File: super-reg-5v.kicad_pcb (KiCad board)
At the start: 2 copper layers, 85 x 35 mm, 49 parts, among them J1 SENS_IN, Q1 2SA1015GR, Q2 D44H11, U1 LM317T, U3 AD825, X1 AC_IN, X2 DC_OUT

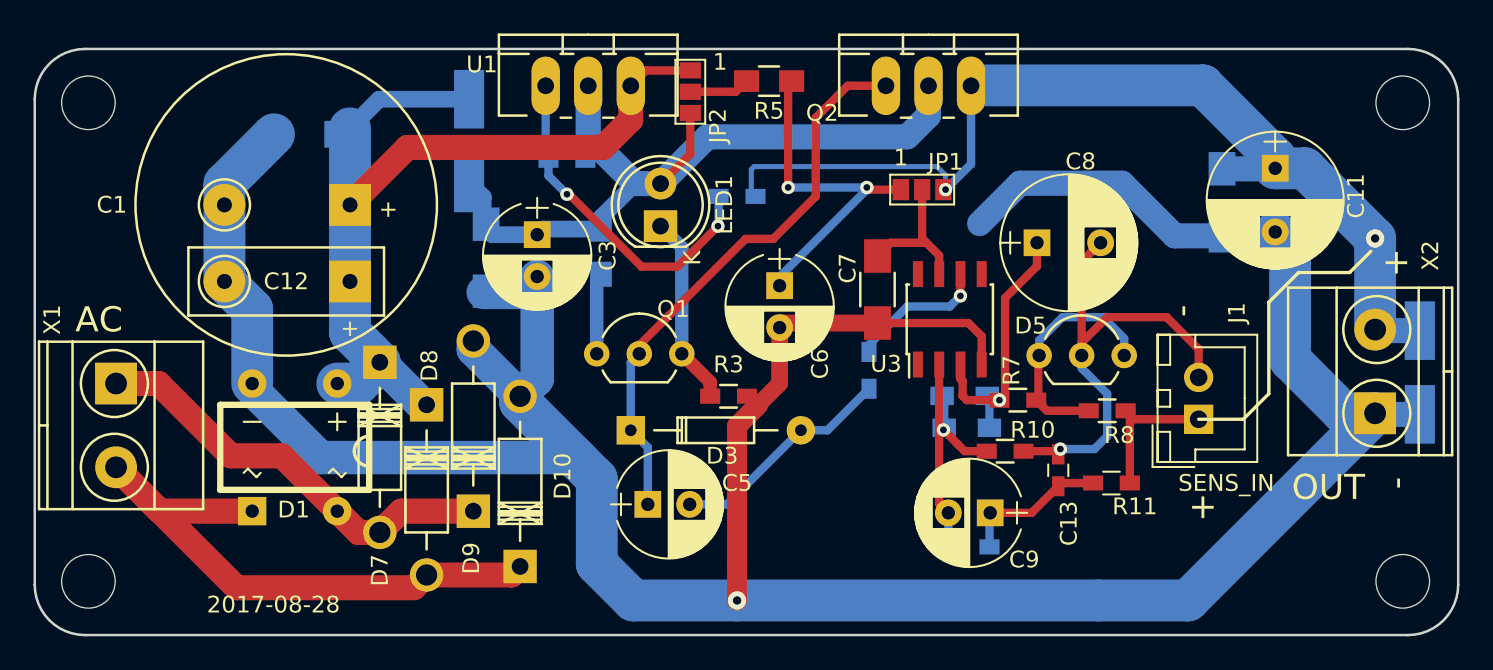
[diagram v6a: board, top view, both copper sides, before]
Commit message: add masks fix silks
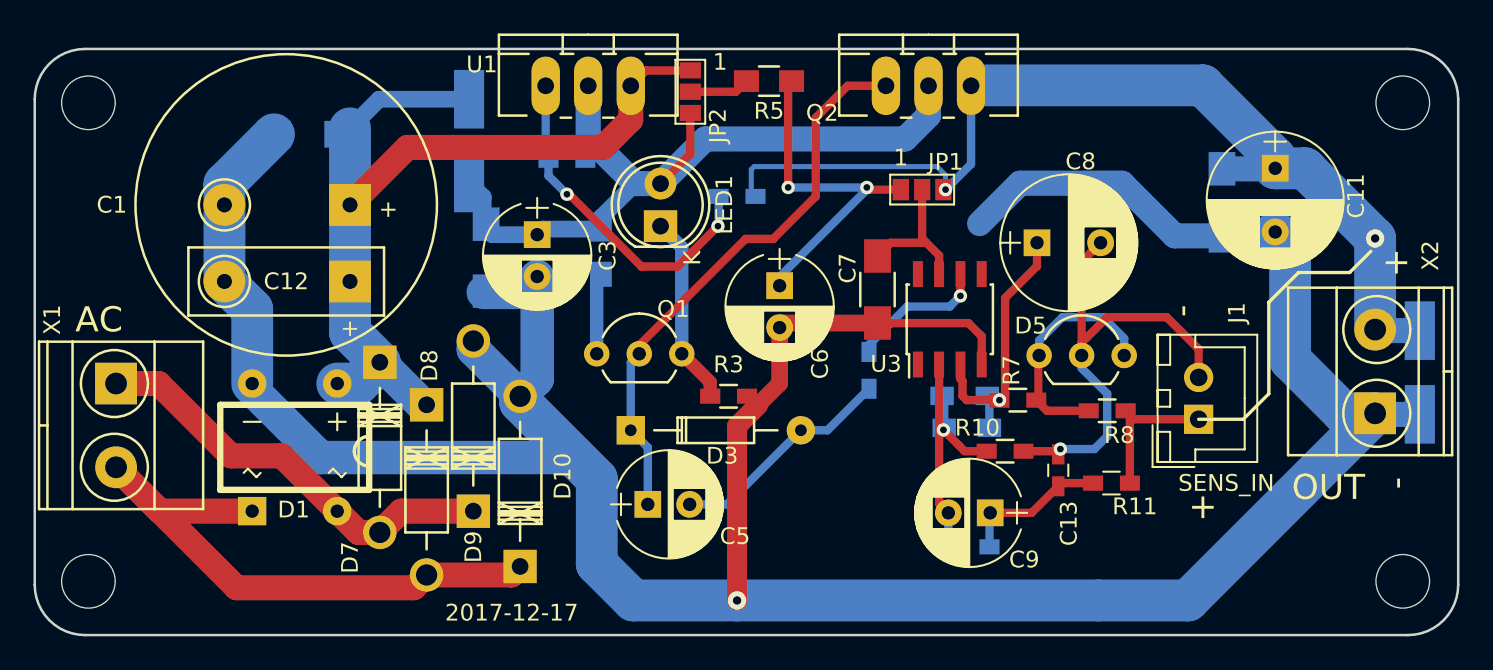
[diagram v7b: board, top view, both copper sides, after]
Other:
- board text added: "2017-12-17"
- board text removed: "2017-08-28"
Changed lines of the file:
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@@
     (area 112.924999 73.924999 198.075001 109.075001)
     (thickness 1.6)
-    (drawings 32)
+    (drawings 80)
     (tracks 247)
     (zones 0)
@@
   )
   (setup
-    (last_trace_width 0.5)
+    (last_trace_width 0.25)
     (user_trace_width 0.3)
     (user_trace_width 0.5)
@@
     (zone_45_only no)
     (trace_min 0.25)
-    (segment_width 1.2)
+    (segment_width 1.5)
     (edge_width 0.15)
     (via_size 0.8)
@@
     (tags "resistor 0603")
     (attr smd)
-    (fp_text reference R1 (at 0.254 1.524 180) (layer B.SilkS)
+    (fp_text reference R1 (at 0.506 1.676 180) (layer B.SilkS)
       (effects (font (size 1 1) (thickness 0.15)) (justify mirror))
     )
@@
     (tags "resistor 0603")
     (attr smd)
-    (fp_text reference R9 (at 0 -1.524 180) (layer B.SilkS)
+    (fp_text reference R9 (at 0 -1.397 180) (layer B.SilkS)
       (effects (font (size 1 1) (thickness 0.15)) (justify mirror))
     )
@@
     (tags "resistor 0603")
     (attr smd)
-    (fp_text reference R10 (at 1.651 -1.27) (layer F.SilkS)
+    (fp_text reference R10 (at -1.651 -1.397) (layer F.SilkS)
       (effects (font (size 1 1) (thickness 0.15)))
     )
@@
     (descr "Diode, DO-41, SOD81, Horizontal, RM 10mm,")
     (tags "Diode, DO-41, SOD81, Horizontal, RM 10mm, 1N4007, SB140,")
-    (fp_text reference D7 (at 12.421 -0.002 270) (layer F.SilkS)
+    (fp_text reference D7 (at 11.659 1.776 270) (layer F.SilkS)
       (effects (font (size 1 1) (thickness 0.15)))
     )
@@
     (descr "Diode, DO-41, SOD81, Horizontal, RM 10mm,")
     (tags "Diode, DO-41, SOD81, Horizontal, RM 10mm, 1N4007, SB140,")
-    (fp_text reference D9 (at -2.814 -0.122 90) (layer F.SilkS)
+    (fp_text reference D9 (at -2.134 0.002 90) (layer F.SilkS)
       (effects (font (size 1 1) (thickness 0.15)))
     )
@@
     (descr "CP, Radial series, Radial, pin pitch=2.50mm, , diameter=6.3mm, Electrolytic Capacitor")
     (tags "CP Radial series Radial pin pitch 2.50mm  diameter 6.3mm Electrolytic Capacitor")
-    (fp_text reference C5 (at 5.334 -1.27) (layer F.SilkS)
+    (fp_text reference C5 (at 5.207 1.905) (layer F.SilkS)
       (effects (font (size 1 1) (thickness 0.15)))
     )
@@
     )
   )
+  (gr_line (start 150.37 82.017) (end 153.037 79.35) (angle 90) (layer B.Mask) (width 1.5))
+  (gr_line (start 166.372 77.953) (end 164.975 79.35) (angle 90) (layer B.Mask) (width 1.5))
+  (gr_line (start 164.848 79.35) (end 153.037 79.35) (angle 90) (layer B.Mask) (width 1.5))
+  (gr_line (start 166.372 77.953) (end 166.372 76.175) (angle 90) (layer B.Mask) (width 1.5))
+  (gr_line (start 148.846 82.017) (end 150.37 82.017) (angle 90) (layer B.Mask) (width 1.5))
+  (gr_line (start 146.052 79.223) (end 148.846 82.017) (angle 90) (layer B.Mask) (width 1.5))
+  (gr_line (start 146.052 76.175) (end 146.052 79.223) (angle 90) (layer B.Mask) (width 1.5))
+  (gr_line (start 125.859 101.575) (end 120.906 101.575) (angle 90) (layer F.Mask) (width 1.5))
+  (gr_line (start 136.273 95.352) (end 133.733 92.812) (angle 90) (layer B.Mask) (width 2))
+  (gr_line (start 139.194 91.923) (end 141.734 94.463) (angle 90) (layer B.Mask) (width 2))
+  (gr_line (start 139.194 91.415) (end 139.194 91.923) (angle 90) (layer B.Mask) (width 2))
+  (gr_line (start 130.05 98.4) (end 145.29 98.4) (angle 90) (layer B.Mask) (width 2))
+  (gr_line (start 125.732 94.082) (end 130.05 98.4) (angle 90) (layer B.Mask) (width 2))
+  (gr_line (start 193.042 85.319) (end 193.042 90.78) (angle 90) (layer B.Mask) (width 2.5))
+  (gr_line (start 188.851 81.128) (end 193.042 85.319) (angle 90) (layer B.Mask) (width 2.5))
+  (gr_line (start 187.2 81.128) (end 188.851 81.128) (angle 90) (layer B.Mask) (width 2.5))
+  (gr_line (start 187.2 80.62) (end 187.2 81.128) (angle 90) (layer B.Mask) (width 2.5))
+  (gr_line (start 182.755 76.175) (end 187.2 80.62) (angle 90) (layer B.Mask) (width 2.5))
+  (gr_line (start 169.801 76.175) (end 182.755 76.175) (angle 90) (layer B.Mask) (width 2.5))
+  (gr_line (start 181.866 106.909) (end 193.042 95.733) (angle 90) (layer B.Mask) (width 2.5))
+  (gr_line (start 148.719 106.909) (end 181.866 106.909) (angle 90) (layer B.Mask) (width 2.5))
+  (gr_line (start 146.56 104.75) (end 148.719 106.909) (angle 90) (layer B.Mask) (width 2.5))
+  (gr_line (start 146.56 99.543) (end 146.56 104.75) (angle 90) (layer B.Mask) (width 2.5))
+  (gr_line (start 141.988 95.098) (end 146.56 99.67) (angle 90) (layer B.Mask) (width 2.5))
+  (gr_line (start 141.988 94.717) (end 141.988 95.098) (angle 90) (layer B.Mask) (width 2.5))
+  (gr_line (start 132.336 93.955) (end 131.066 93.955) (angle 90) (layer B.Mask) (width 2.5))
+  (gr_line (start 133.606 92.685) (end 132.336 93.955) (angle 90) (layer B.Mask) (width 2.5))
+  (gr_line (start 131.828 90.907) (end 133.606 92.685) (angle 90) (layer B.Mask) (width 2.5))
+  (gr_line (start 131.828 83.414) (end 131.828 90.907) (angle 90) (layer B.Mask) (width 2.5))
+  (gr_line (start 125.986 89.51) (end 125.986 93.955) (angle 90) (layer B.Mask) (width 2.5))
+  (gr_line (start 124.335 87.859) (end 125.986 89.51) (angle 90) (layer B.Mask) (width 2.5))
+  (gr_line (start 124.335 83.287) (end 124.335 87.986) (angle 90) (layer B.Mask) (width 2.5))
+  (gr_line (start 141.48 105.385) (end 141.988 104.877) (angle 90) (layer F.Mask) (width 1.5))
+  (gr_line (start 136.4 105.385) (end 141.48 105.385) (angle 90) (layer F.Mask) (width 1.5))
+  (gr_line (start 135.638 106.147) (end 136.4 105.385) (angle 90) (layer F.Mask) (width 1.5))
+  (gr_line (start 125.097 106.147) (end 135.638 106.147) (angle 90) (layer F.Mask) (width 1.5))
+  (gr_line (start 117.858 99.035) (end 125.097 106.274) (angle 90) (layer F.Mask) (width 1.5))
+  (gr_line (start 134.876 101.575) (end 139.194 101.575) (angle 90) (layer F.Mask) (width 1.5))
+  (gr_line (start 133.606 102.845) (end 134.876 101.575) (angle 90) (layer F.Mask) (width 1.5))
+  (gr_line (start 132.336 102.845) (end 133.606 102.845) (angle 90) (layer F.Mask) (width 1.5))
+  (gr_line (start 127.764 98.273) (end 132.336 102.845) (angle 90) (layer F.Mask) (width 1.5))
+  (gr_line (start 124.716 98.273) (end 127.764 98.273) (angle 90) (layer F.Mask) (width 1.5))
+  (gr_line (start 120.398 93.955) (end 124.716 98.273) (angle 90) (layer F.Mask) (width 1.5))
+  (gr_line (start 117.858 93.955) (end 120.398 93.955) (angle 90) (layer F.Mask) (width 1.5))
+  (gr_line (start 148.592 78.207) (end 148.592 76.175) (angle 90) (layer F.Mask) (width 1.5))
+  (gr_line (start 146.941 79.858) (end 148.592 78.207) (angle 90) (layer F.Mask) (width 1.5))
+  (gr_line (start 135.257 79.858) (end 146.941 79.858) (angle 90) (layer F.Mask) (width 1.5))
+  (gr_line (start 131.828 83.287) (end 135.257 79.858) (angle 90) (layer F.Mask) (width 1.5))
   (gr_line (start 193.05 85.319) (end 193.02 85.319) (angle 90) (layer F.Mask) (width 1.2))
   (gr_text * (at 136.527 75.032) (layer B.SilkS)
@@
   (gr_arc (start 116 106) (end 116 109) (angle 90) (layer Edge.Cuts) (width 0.15))
   (gr_arc (start 116 77) (end 113 77) (angle 90) (layer Edge.Cuts) (width 0.15))
-  (gr_text 2017-08-28 (at 127.254 107.188) (layer F.SilkS)
+  (gr_text 2017-12-17 (at 141.48 107.671) (layer F.SilkS)
     (effects (font (size 1 1) (thickness 0.15)))
   )
@@
   (segment (start 140.33 85.09) (end 139.7782 84.5382) (width 1) (layer B.Cu) (net 3))
   (segment (start 166.37 76.2) (end 166.37 77.978) (width 1.5) (layer B.Cu) (net 3))
-  (segment (start 153.162 79.248) (end 150.368 82.042) (width 1.5) (layer B.Cu) (net 3))
-  (segment (start 165.1 79.248) (end 153.162 79.248) (width 1.5) (layer B.Cu) (net 3))
-  (segment (start 166.37 77.978) (end 165.1 79.248) (width 1.5) (layer B.Cu) (net 3))
+  (segment (start 153.035 79.375) (end 150.368 82.042) (width 1.5) (layer B.Cu) (net 3))
+  (segment (start 164.973 79.375) (end 153.035 79.375) (width 1.5) (layer B.Cu) (net 3))
+  (segment (start 166.37 77.978) (end 164.973 79.375) (width 1.5) (layer B.Cu) (net 3))
   (segment (start 145.88 80.645) (end 145.88 79.418) (width 0.8) (layer B.Cu) (net 3))
   (segment (start 145.88 79.418) (end 146.05 79.248) (width 0.8) (layer B.Cu) (net 3))
@@
   (segment (start 154.32798 101.194) (end 158.75052 96.77146) (width 0.5) (layer B.Cu) (net 4))
   (segment (start 159.06998 96.452) (end 158.75052 96.77146) (width 0.8) (layer B.Cu) (net 4))
-  (segment (start 164.721 82.398) (end 162.816 82.398) (width 0.5) (layer F.Cu) (net 5) (status 400000))
+  (segment (start 164.721 82.398) (end 162.816 82.398) (width 0.5) (layer F.Cu) (net 5))
   (via (at 162.689 82.271) (size 0.8) (drill 0.4) (layers F.Cu B.Cu) (net 5))
   (segment (start 162.689 82.271) (end 162.587 82.169) (width 0.5) (layer B.Cu) (net 5))

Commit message: update transistor package changes for opams power
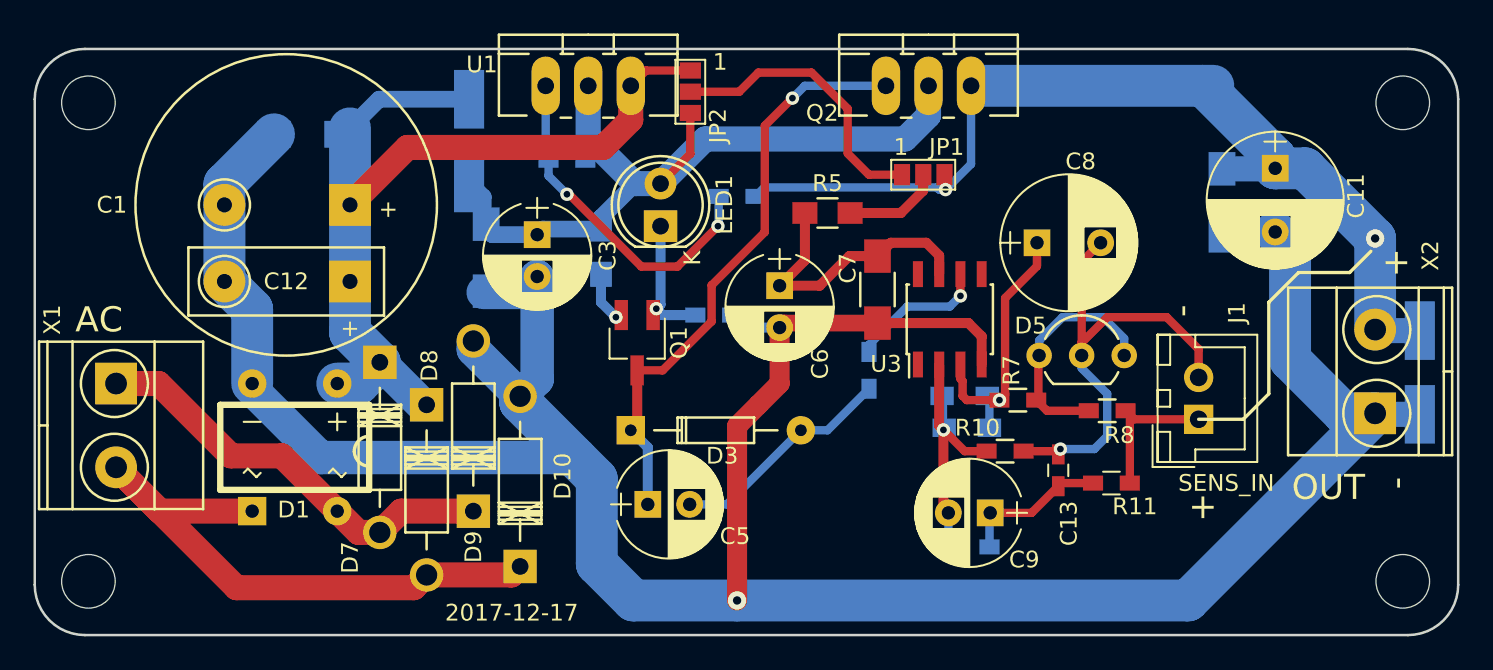
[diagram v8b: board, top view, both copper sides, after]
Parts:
- Q1: value 2SA1015GR -> 2SA1162GR; footprint TO_SOT_Packages_THT:TO-92_Inline_Wide -> TO_SOT_Packages_SMD:SC-59_Handsoldering
- R3: moved to B.Cu
- moved R5 8.61 mm to (160.3, 83.8), turned to 0 degrees
- moved R3 4.93 mm to (153.5, 89.9)
- moved Q1 2.50 mm to (149.0, 91.5), turned to 270 degrees
- moved JP1 0.89 mm to (166.1, 81.5)
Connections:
- C6 pad 1: Net-(C6-Pad1) -> /OPAMP_PW
- JP1 pad 1: Net-(C6-Pad1) -> Net-(JP1-Pad1)
- JP1 pad 2: /OPAMP_PW -> Net-(JP1-Pad2)
- JP2 pad 2: Net-(JP2-Pad2) -> Net-(JP1-Pad1)
- Q1 pad 1: Net-(Q1-Pad1) -> Net-(LED1-Pad1)
- Q1 pad 2: Net-(C5-Pad1) -> Net-(Q1-Pad2)
- Q1 pad 3: Net-(LED1-Pad1) -> Net-(C5-Pad1)
- R4 pad 2: Net-(Q1-Pad1) -> Net-(Q1-Pad2)
- R5 pad 1: Net-(C6-Pad1) -> /OPAMP_PW
- R5 pad 2: Net-(JP2-Pad2) -> Net-(JP1-Pad2)
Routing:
- net Net-(C6-Pad1): track 21.6 -> 0.00 mm, vias 2 -> 0
- net Net-(JP1-Pad1): track 0.00 -> 17.2 mm
- net GND: track 186.9 -> 172.4 mm
- net /OPAMP_PW: track 8.72 -> 17.0 mm
- net Net-(JP1-Pad2): track 0.00 -> 5.87 mm
- net Net-(Q1-Pad1): track 4.85 -> 0.00 mm
- net Net-(JP2-Pad2): track 3.61 -> 0.00 mm
- net Net-(LED1-Pad1): track 11.4 -> 7.98 mm, vias 0 -> 1
- net Net-(Q1-Pad2): track 0.00 -> 3.30 mm, vias 0 -> 1
- net Net-(C5-Pad1): track 35.3 -> 35.5 mm, vias 0 -> 1
